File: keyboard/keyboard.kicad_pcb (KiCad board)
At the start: 2 copper layers, 64 parts, among them SW1 MX_SW_HS, SW10 MX_SW_HS, SW11 MX_SW_HS, SW12 MX_SW_HS, SW13 MX_SW_HS, SW14 MX_SW_HS, SW15 MX_SW_HS, SW16 MX_SW_HS, SW17 MX_SW_HS, SW18 MX_SW_HS, SW19 MX_SW_HS, SW2 MX_SW_HS, SW20 MX_SW_HS, SW21 MX_SW_HS, SW22 MX_SW_HS, SW23 MX_SW_HS, SW24 MX_SW_HS, SW25 MX_SW_HS, SW26 MX_SW_HS, SW27 MX_SW_HS, SW28 MX_SW_HS, SW29 MX_SW_HS, SW3 MX_SW_HS, SW30 MX_SW_HS, SW31 MX_SW_HS, SW32 MX_SW_HS, SW33 MX_SW_HS, SW34 MX_SW_HS, SW35 MX_SW_HS, SW36 MX_SW_HS, SW37 MX_SW_HS, SW38 MX_SW_HS, SW39 MX_SW_HS, SW4 MX_SW_HS, SW40 MX_SW_HS, SW41 MX_SW_HS, SW42 MX_SW_HS, SW43 MX_SW_HS, SW44 MX_SW_HS, SW45 MX_SW_HS, SW46 MX_SW_HS, SW47 MX_SW_HS, SW48 MX_SW_HS, SW49 MX_SW_HS, SW5 MX_SW_HS, SW50 MX_SW_HS, SW51 MX_SW_HS, SW52 MX_SW_HS, SW53 MX_SW_HS, SW54 MX_SW_HS, SW55 MX_SW_HS, SW56 MX_SW_HS, SW57 MX_SW_HS, SW58 MX_SW_HS, SW59 MX_SW_HS, SW6 MX_SW_HS, SW60 MX_SW_HS, SW61 MX_SW_HS, SW62 MX_SW_HS, SW63 MX_SW_HS, SW64 MX_SW_HS, SW7 MX_SW_HS, SW8 MX_SW_HS, SW9 MX_SW_HS

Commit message: Place the keys on the PCB
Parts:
- SW1, SW10, SW11, SW12, SW13, SW14, SW15, SW16, SW17, SW18, SW19, SW2, SW20, SW21, SW22, SW23, SW24, SW25, SW26, SW27, SW28, SW29, SW3, SW30, SW31, SW32, SW33, SW34, SW35, SW36, SW37, SW38, SW39, SW4, SW40, SW41, SW42, SW43, SW44, SW45, SW46, SW47, SW48, SW49, SW5, SW50, SW51, SW52, SW53, SW54, SW55, SW56, SW57, SW58, SW59, SW6, SW60, SW61, SW62, SW63, SW64, SW7, SW8, SW9: moved to B.Cu
- moved SW43 455.0 mm to (509.6, 104.8), turned to 180 degrees
- moved SW21 453.3 mm to (509.6, 66.7), turned to 180 degrees
- moved SW11 435.5 mm to (523.9, 47.6), turned to 180 degrees
- moved SW54 426.0 mm to (514.4, 123.8), turned to 180 degrees
- moved SW51 421.4 mm to (457.2, 123.8), turned to 180 degrees
- moved SW18 416.5 mm to (452.4, 66.7), turned to 180 degrees
- moved SW22 413.9 mm to (528.6, 66.7), turned to 180 degrees
- moved SW63 412.7 mm to (504.8, 142.9), turned to 180 degrees
- moved SW31 408.5 mm to (485.8, 85.7), turned to 180 degrees
- moved SW62 408.4 mm to (485.8, 142.9), turned to 180 degrees
- moved SW64 406.2 mm to (523.9, 142.9), turned to 180 degrees
- moved SW19 394.2 mm to (471.5, 66.7), turned to 180 degrees
- moved SW6 387.1 mm to (428.6, 47.6), turned to 180 degrees
- moved SW53 380.6 mm to (495.3, 123.8), turned to 180 degrees
- moved SW40 378.6 mm to (452.4, 104.8), turned to 180 degrees
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
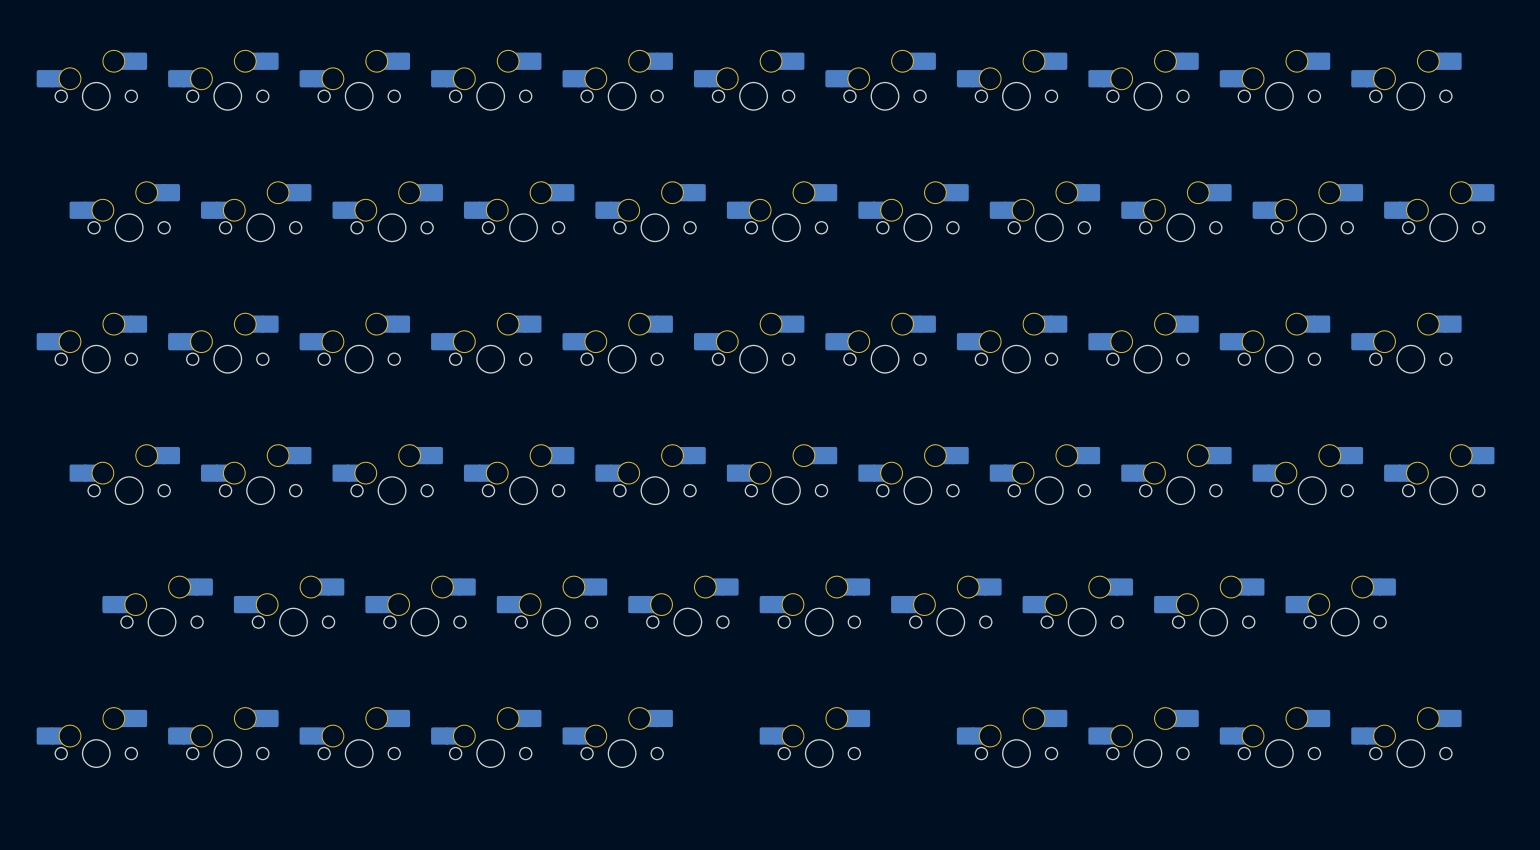
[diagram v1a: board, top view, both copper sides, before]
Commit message: Add an edge cut
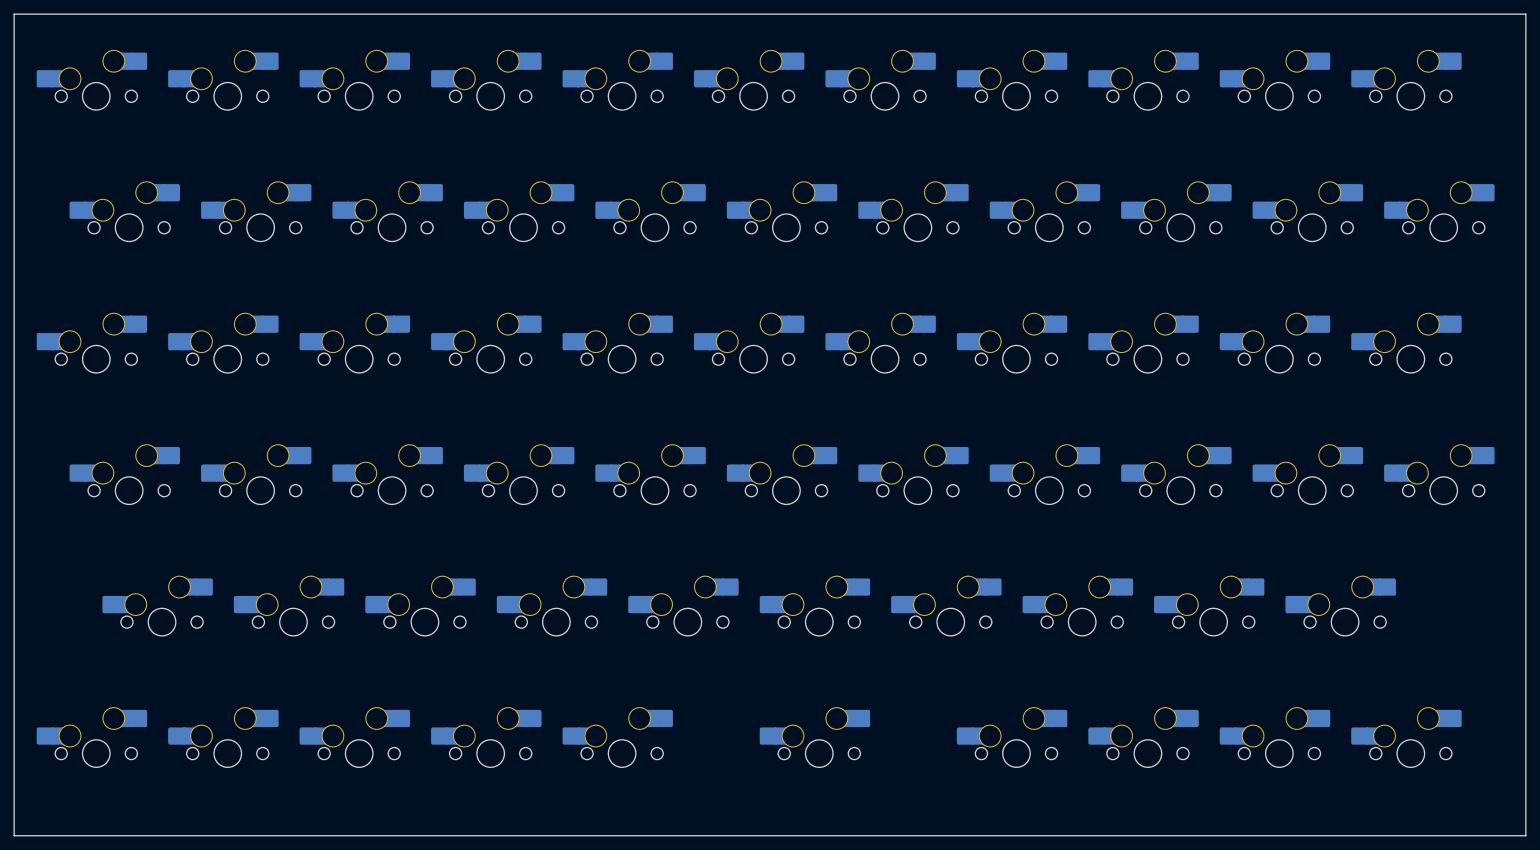
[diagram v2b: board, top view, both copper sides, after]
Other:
- board outline added: 219.1 x 119.1 mm
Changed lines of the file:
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@@
     )
   )
+  (gr_line (start 321.46875 35.71875) (end 321.46875 154.78125) (layer "Edge.Cuts") (width 0.1))
+  (gr_line (start 321.46875 154.78125) (end 540.54375 154.78125) (layer "Edge.Cuts") (width 0.1))
+  (gr_line (start 540.54375 154.78125) (end 540.54375 35.71875) (layer "Edge.Cuts") (width 0.1))
+  (gr_line (start 540.54375 35.71875) (end 321.46875 35.71875) (layer "Edge.Cuts") (width 0.1))
 )

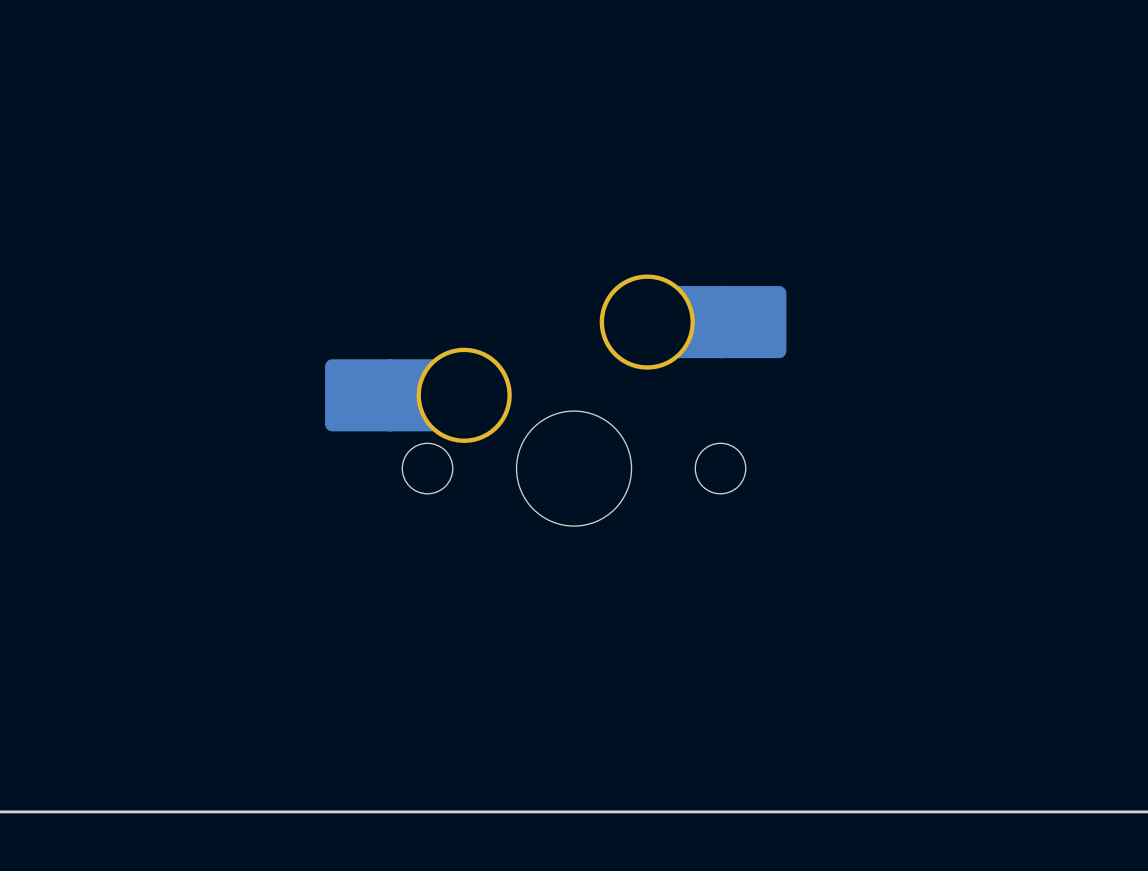
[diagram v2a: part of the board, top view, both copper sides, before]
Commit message: Add stabiliser
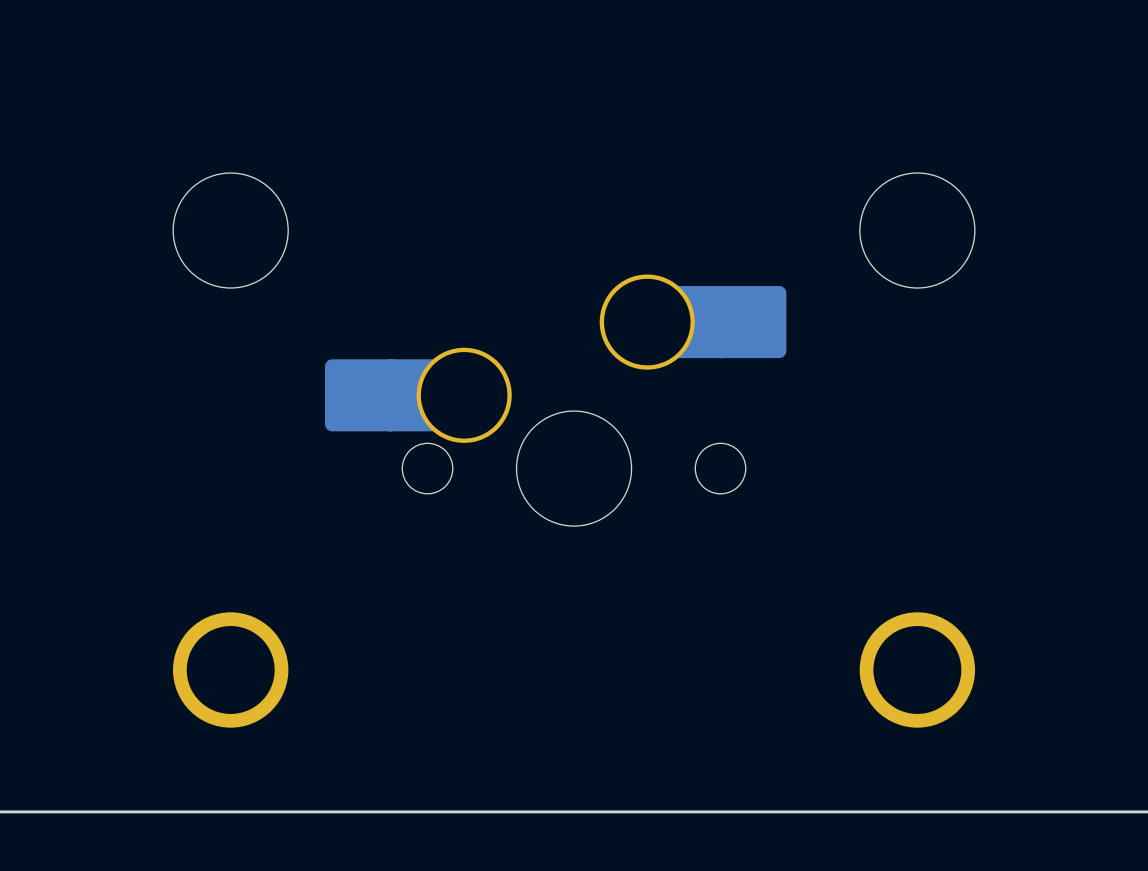
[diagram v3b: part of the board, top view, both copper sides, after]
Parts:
- added S1: MX_stab, marbastlib-mx:STAB_MX_P_2u, F.Cu at (438.1, 142.9)
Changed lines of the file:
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@@
   (net 127 "unconnected-(SW64-Pad1)")
   (net 128 "unconnected-(SW64-Pad2)")
+  (footprint "marbastlib-mx:STAB_MX_P_2u" (layer "F.Cu")
+    (at 438.15 142.875 180)
+    (descr "Footprint for Cherry Clip/Screw in type stabilizers, 2u")
+    (property "Sheetfile" "keyboard.kicad_sch")
+    (property "Sheetname" "")
+    (attr through_hole exclude_from_pos_files)
+    (fp_text reference "S1" (at 0 0) (layer "F.SilkS") hide
+      (effects (font (size 1 1) (thickness 0.15)))
+    )
+    (fp_text value "MX_stab" (at 0 8.128) (layer "F.Fab")
+      (effects (font (size 1 1) (thickness 0.15)))
+    )
+    (fp_line (start 5 -7) (end 7 -7) (layer "Dwgs.User") (width 0.12))
+    (fp_line (start 7 7) (end 7 5) (layer "Dwgs.User") (width 0.12))
+    (fp_line (start -19.05 9.525) (end 19.05 9.525) (layer "Dwgs.User") (width 0.12))
+    (fp_line (start -19.05 -9.525) (end 19.05 -9.525) (layer "Dwgs.User") (width 0.12))
+    (fp_line (start 19.05 -9.525) (end 19.05 9.525) (layer "Dwgs.User") (width 0.12))
+    (fp_line (start -7 -5) (end -7 -7) (layer "Dwgs.User") (width 0.12))
+    (fp_line (start 5 7) (end 7 7) (layer "Dwgs.User") (width 0.12))
+    (fp_line (start -7 7) (end -7 5) (layer "Dwgs.User") (width 0.12))
+    (fp_line (start -19.05 -9.525) (end -19.05 9.525) (layer "Dwgs.User") (width 0.12))
+    (fp_line (start 7 -7) (end 7 -5) (layer "Dwgs.User") (width 0.12))
+    (fp_line (start -7 -7) (end -5 -7) (layer "Dwgs.User") (width 0.12))
+    (fp_line (start -5 7) (end -7 7) (layer "Dwgs.User") (width 0.12))
+    (fp_line (start 9.03125 -5.999999) (end 14.780039 -5.999999) (layer "Eco2.User") (width 0.05))
+    (fp_line (start -14.78125 -5.999999) (end -9.03125 -5.999999) (layer "Eco2.User") (width 0.05))
+    (fp_line (start 15.280039 -5.499999) (end 15.28125 7.500001) (layer "Eco2.User") (width 0.05))
+    (fp_line (start -14.78125 8.000001) (end -9.03125 8.000001) (layer "Eco2.User") (width 0.05))
+    (fp_line (start -15.28125 -5.499999) (end -15.28125 7.500001) (layer "Eco2.User") (width 0.05))
+    (fp_line (start 8.53125 -5.499999) (end 8.53125 7.500001) (layer "Eco2.User") (width 0.05))
+    (fp_line (start -8.53125 -5.499999) (end -8.53125 7.500001) (layer "Eco2.User") (width 0.05))
+    (fp_line (start 9.03125 8.000001) (end 14.78125 8.000001) (layer "Eco2.User") (width 0.05))
+    (fp_arc (start -15.28125 -5.499999) (mid -15.134803 -5.853552) (end -14.78125 -5.999999) (layer "Eco2.User") (width 0.05))
+    (fp_arc (start 15.28125 7.500001) (mid 15.134803 7.853554) (end 14.78125 8.000001) (layer "Eco2.User") (width 0.05))
+    (fp_arc (start -14.78125 8.000001) (mid -15.134803 7.853554) (end -15.28125 7.500001) (layer "Eco2.User") (width 0.05))
+    (fp_arc (start -8.53125 7.500001) (mid -8.677697 7.853554) (end -9.03125 8.000001) (layer "Eco2.User") (width 0.05))
+    (fp_arc (start 8.53125 -5.499999) (mid 8.677697 -5.853552) (end 9.03125 -5.999999) (layer "Eco2.User") (width 0.05))
+    (fp_arc (start 14.780039 -5.999999) (mid 15.133592 -5.853552) (end 15.280039 -5.499999) (layer "Eco2.User") (width 0.05))
+    (fp_arc (start -9.03125 -5.999999) (mid -8.677697 -5.853552) (end -8.53125 -5.499999) (layer "Eco2.User") (width 0.05))
+    (fp_arc (start 9.03125 8.000001) (mid 8.677697 7.853554) (end 8.53125 7.500001) (layer "Eco2.User") (width 0.05))
+    (pad "" thru_hole circle (at -11.90625 -6.985 180) (size 4 4) (drill 3.048) (layers *.Cu "B.Mask"))
+    (pad "" np_thru_hole circle (at -11.90625 8.255 180) (size 3.9878 3.9878) (drill 3.9878) (layers *.Cu *.Mask))
+    (pad "" thru_hole circle (at 11.90625 -6.985 180) (size 4 4) (drill 3.048) (layers *.Cu "B.Mask"))
+    (pad "" np_thru_hole circle (at 11.90625 8.255 180) (size 3.9878 3.9878) (drill 3.9878) (layers *.Cu *.Mask))
+    (group "" (id 5e0cac80-db5c-4015-b0f7-b0e1ee41f2f6)
+      (members
+        14554e89-22f7-424e-b898-2947880697c9
+        1f506e00-c799-46d2-be8e-60cb94b2868e
+        37a9505f-c112-41f2-8d4a-e33cf596d302
+        394cea13-4832-417d-87ae-f6e8d8c173af
+        50fd990f-7466-488d-ab51-f1d2e72efcdf
+        a29a99d9-6770-4599-911b-822fc2b2812f
+        e97d1383-adf4-477b-b16d-54c4f159203e
+        fea560be-28e5-40c4-b7f0-b16b27f1883e
+      )
+    )
+    (group "" (id 91e6310e-b5ef-419f-8415-fe5c3b2212aa)
+      (members
+        0a855fd3-dfe4-4629-bec9-6f40ce5d648b
+        2647d8ac-b445-4095-87a9-0beb4d0a7c05
+        397d6f5c-1209-4f86-b1c2-79746b10ba4c
+        95be5012-020c-4c0d-8391-ab3b5a94dfe5
+        98172e85-e096-48d7-8246-1d5865326208
+        f3defba4-7011-4eba-8ebe-13d1a3a8143e
+        f6c1e44d-5dd7-4f02-8681-f9b9159a5cbb
+        fecfd8f6-2f6a-4d8e-9a00-8dc06267691a
+      )
+    )
+  )
   (footprint "marbastlib-mx:SW_MX_HS_1u" (layer "B.Cu")
     (at 376.2375 104.775 180)

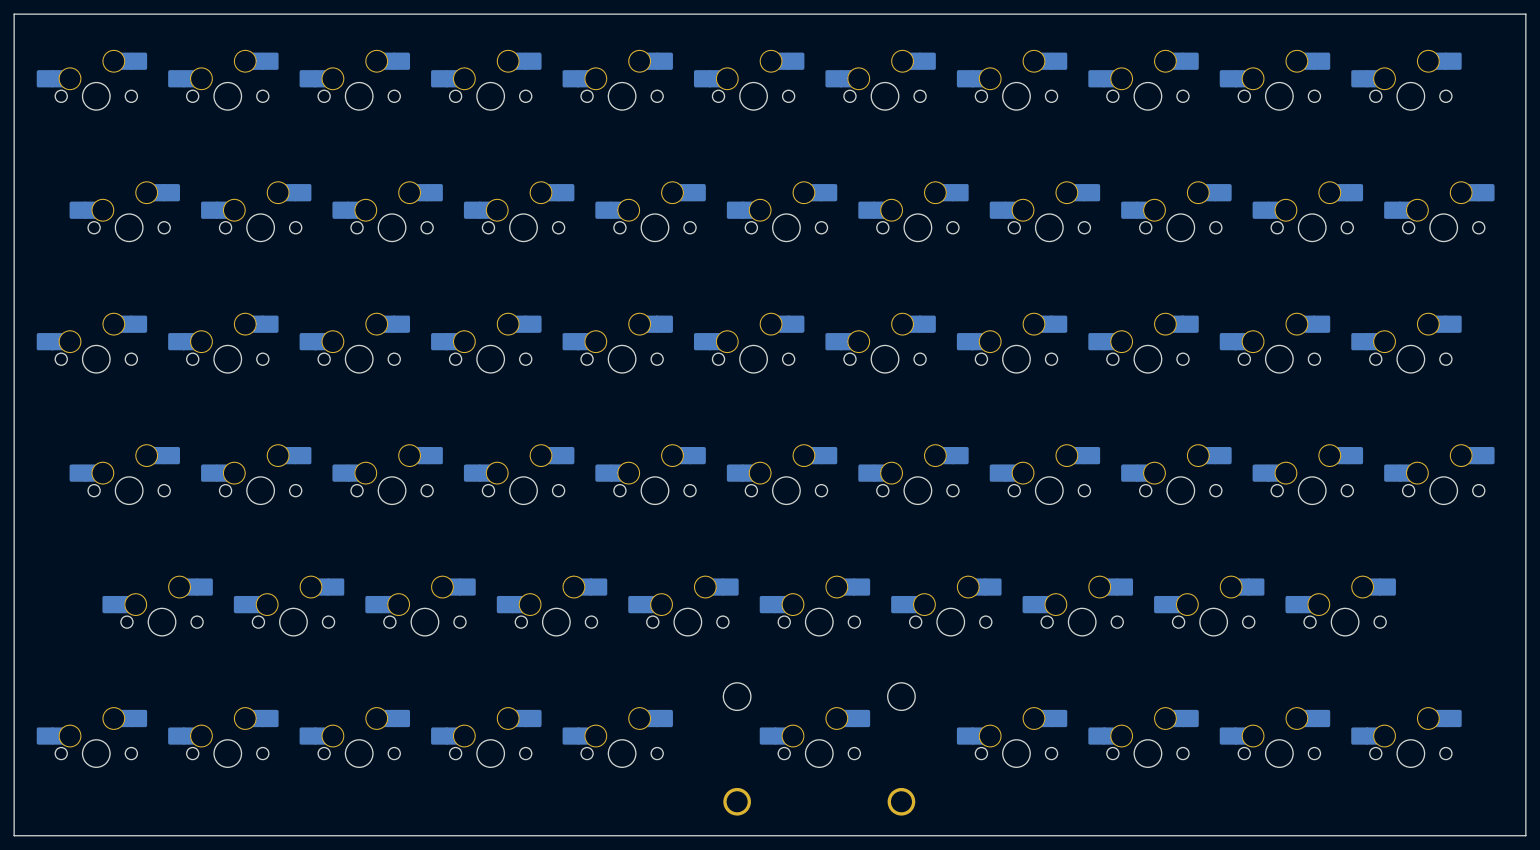
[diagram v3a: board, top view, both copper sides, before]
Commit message: Make the keyboard narrower.
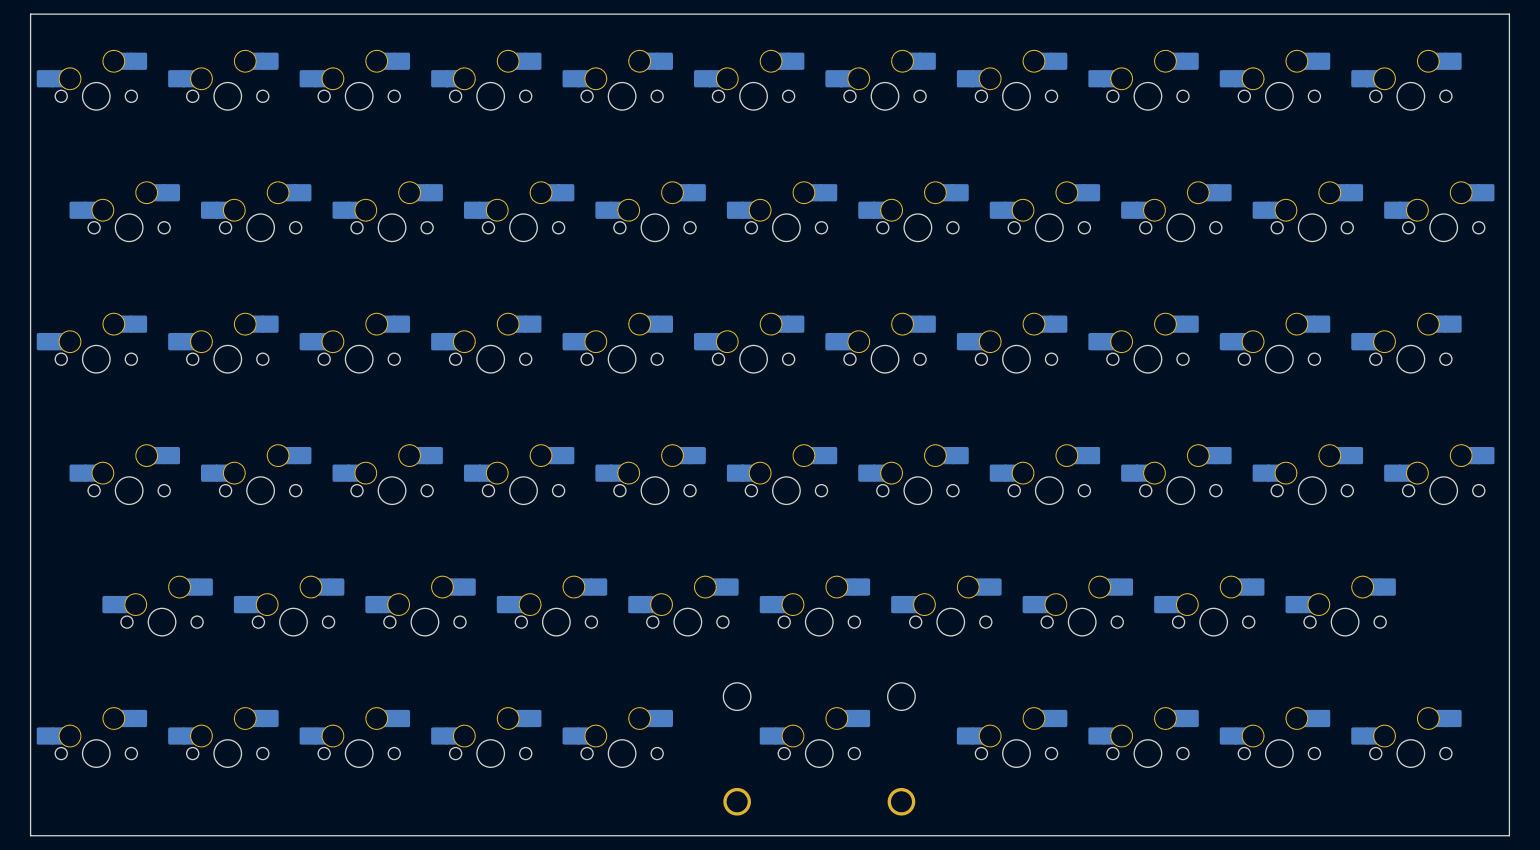
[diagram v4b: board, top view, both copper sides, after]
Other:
- board size 219.1 x 119.1 mm -> 214.3 x 119.1 mm
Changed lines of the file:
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@@
     )
   )
-  (gr_line (start 321.46875 35.71875) (end 321.46875 154.78125) (layer "Edge.Cuts") (width 0.1))
-  (gr_line (start 321.46875 154.78125) (end 540.54375 154.78125) (layer "Edge.Cuts") (width 0.1))
-  (gr_line (start 540.54375 154.78125) (end 540.54375 35.71875) (layer "Edge.Cuts") (width 0.1))
-  (gr_line (start 540.54375 35.71875) (end 321.46875 35.71875) (layer "Edge.Cuts") (width 0.1))
+  (gr_line (start 323.85 35.71875) (end 323.85 154.78125) (layer "Edge.Cuts") (width 0.1))
+  (gr_line (start 323.85 154.78125) (end 538.1625 154.78125) (layer "Edge.Cuts") (width 0.1))
+  (gr_line (start 538.1625 154.78125) (end 538.1625 35.71875) (layer "Edge.Cuts") (width 0.1))
+  (gr_line (start 538.1625 35.71875) (end 323.85 35.71875) (layer "Edge.Cuts") (width 0.1))
 )
